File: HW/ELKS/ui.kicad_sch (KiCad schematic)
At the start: 30 parts

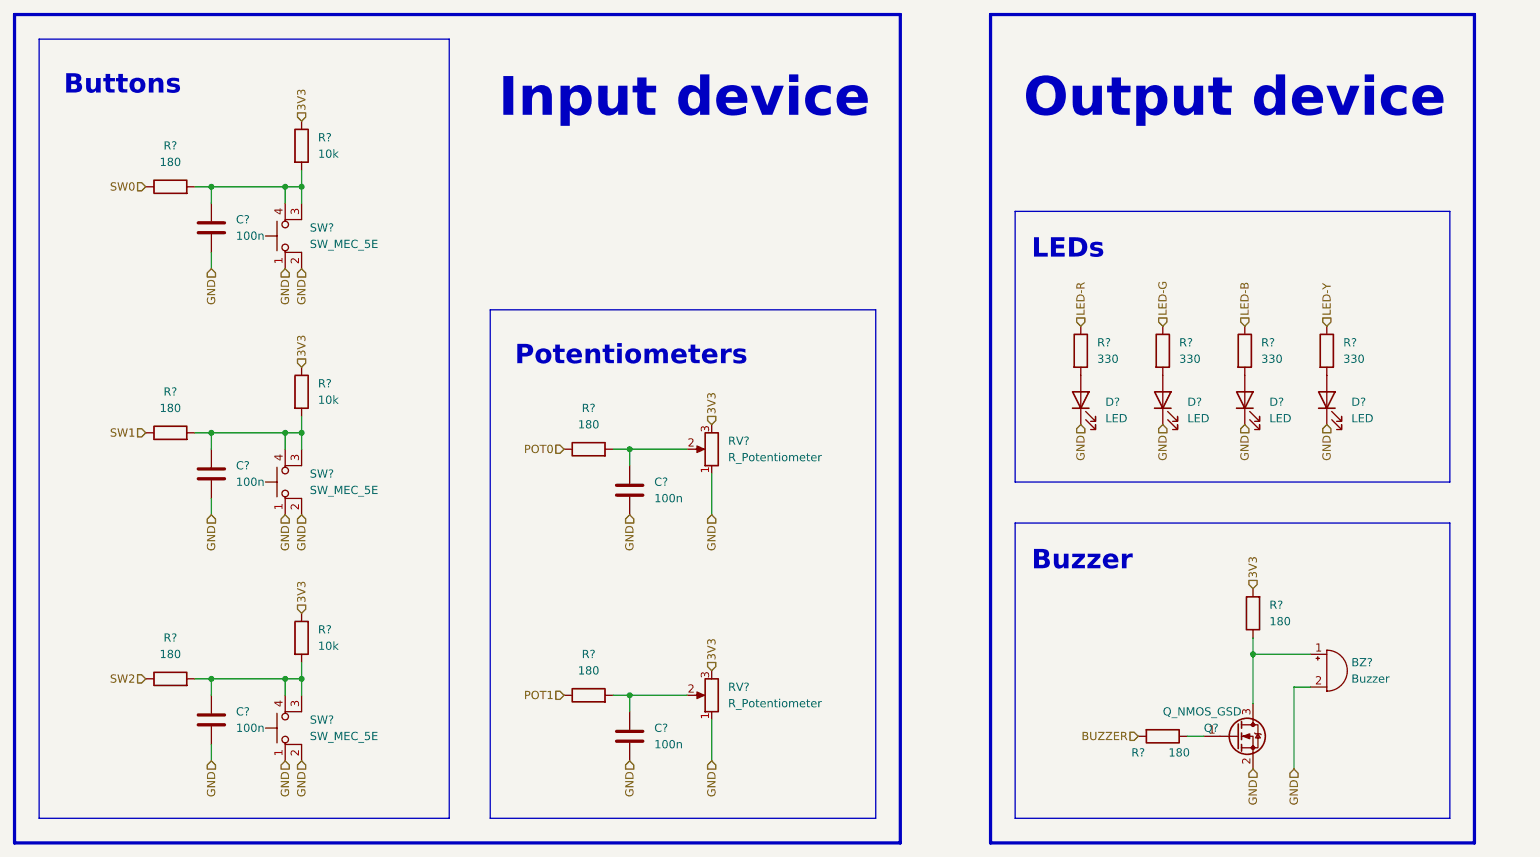
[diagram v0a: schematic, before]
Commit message: Laskakit I2C connector
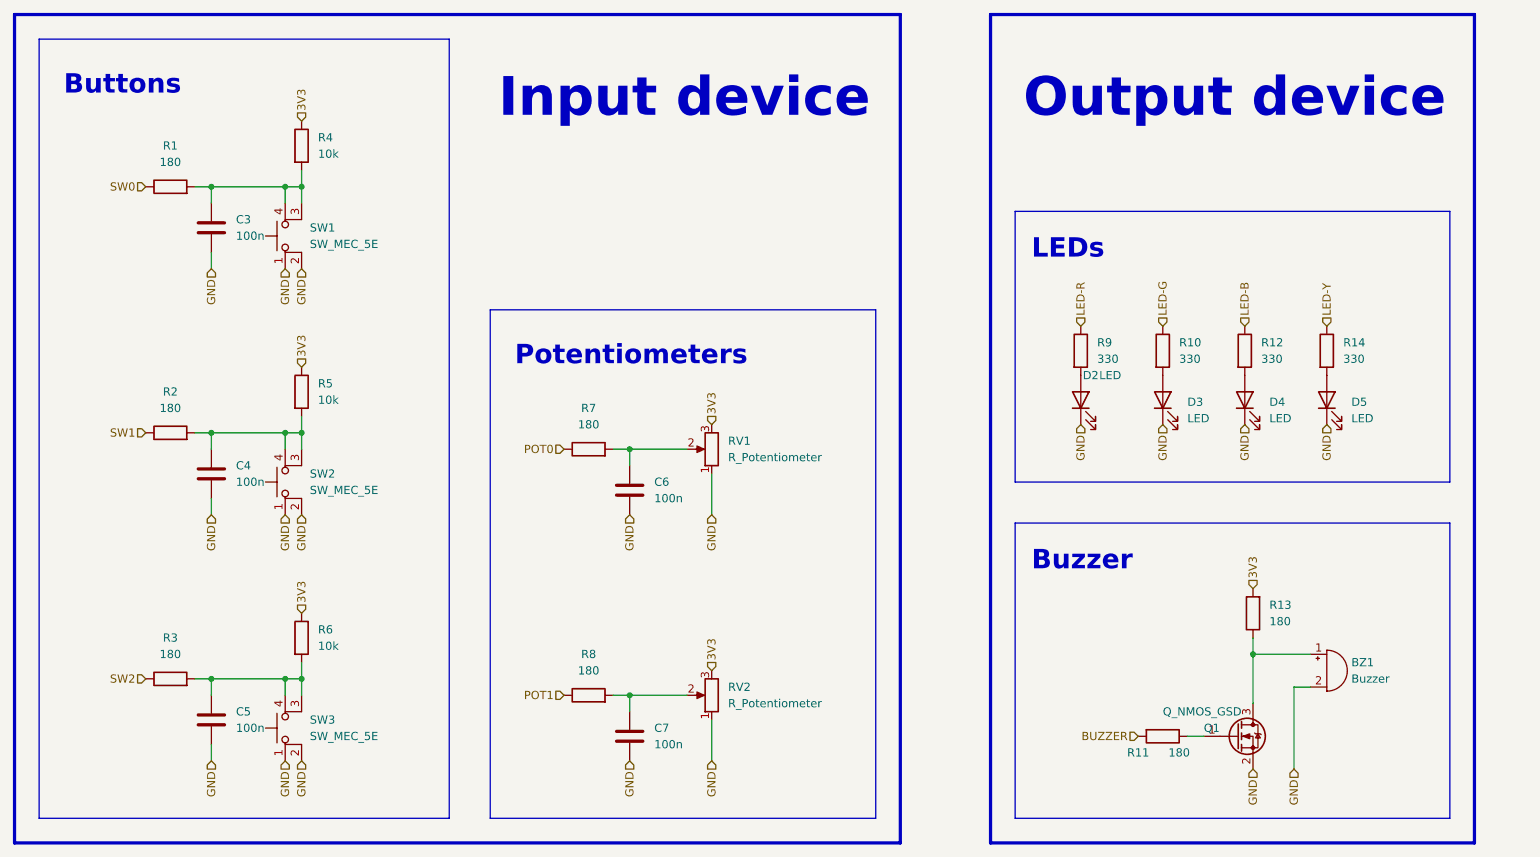
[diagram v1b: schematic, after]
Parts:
- D2, D3, D4, D5: renamed from D?; footprint Connector_USB:USB_C_Receptacle_G-Switch_GT-USB-7010ASV -> LED_SMD:LED_0603_1608Metric
- SW1, SW2, SW3: renamed from SW?; footprint Button_Switch_SMD:SW_Push_1P1T_NO_CK_KSC7xxJ -> Robotarna_KiCad_Library:Tactile_switch
- gave numbers to parts that had none: 23
